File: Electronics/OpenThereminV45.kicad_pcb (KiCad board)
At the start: 2 copper layers, 50.5 x 128.5 mm, 107 parts, among them J1 USB_C_Receptacle 12401610E4#2A, J2 Conn_02x03_Odd_Even, J3 Conn_02x05_Odd_Even, P1 10k, P10 BUTTON, P11 A3_PAD, P12 A2_PAD, P13 A1_PAD, P14 A0_PAD, P16 GND, P2 10k, P3 10k, P4 10k, P8 VCC, P9 GND, U1 TTP223, U10 CH340G, U11 LP2985-3.3, U12 MCP4922-E/SL, U2 74HC4060D, U3 74HC4060D, U4 74HC74, U5 HEF4069, U6 MCP4921-E/SN, U7 MCP4922-E/SL, U8 MCP6002T-I/SN, U9 ATmega328P-AU, X1 16MHz, X2 7.3721MHz, Y1 MountPad3, Y2 MountPad3, Y3 PLUG_3_5_SMD SJ-3502-SMT-TR, Y7 PLUG_3_5_SMD SJ-3502-SMT-TR

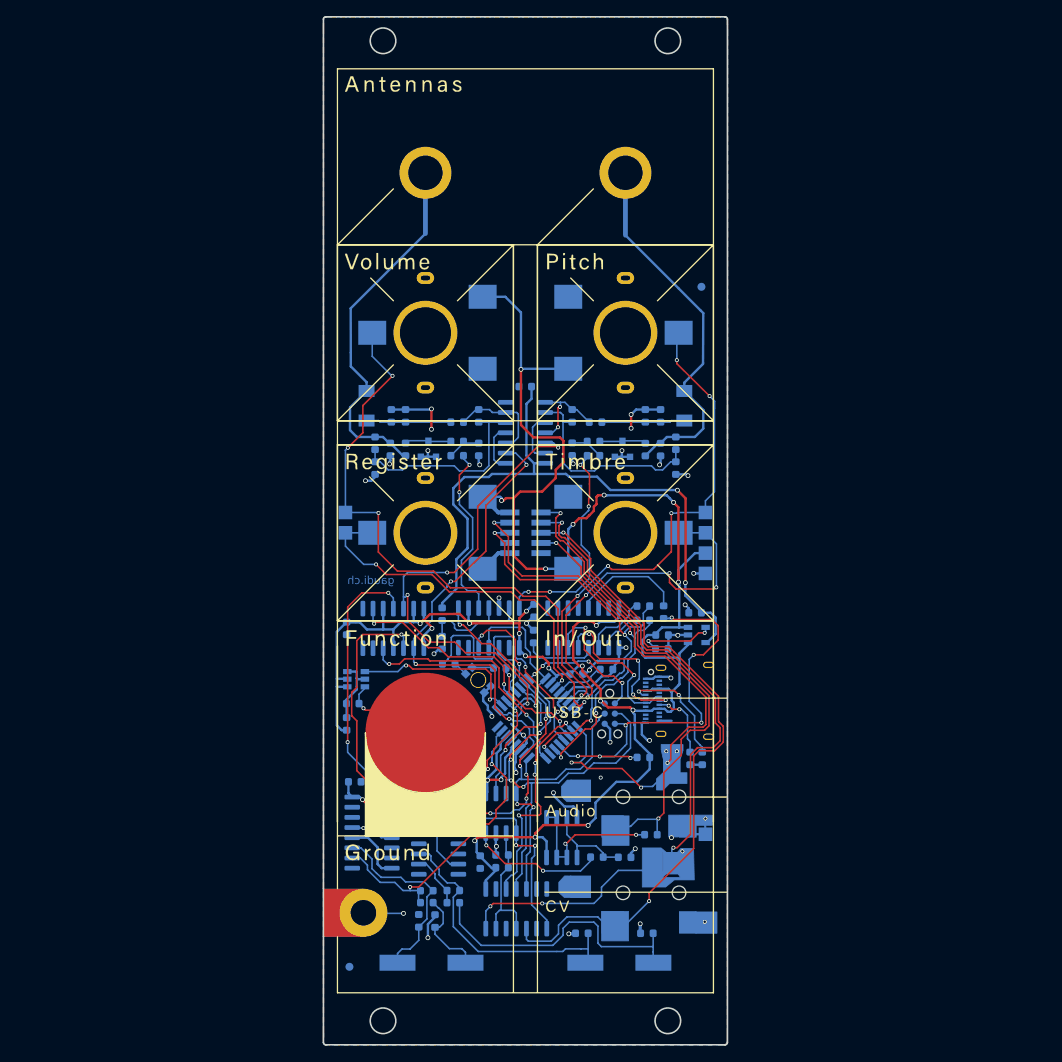
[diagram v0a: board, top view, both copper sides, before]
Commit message: changed to 4-layer and added esd protection and bypass caps
not final yet, audio connector has wrong footprint
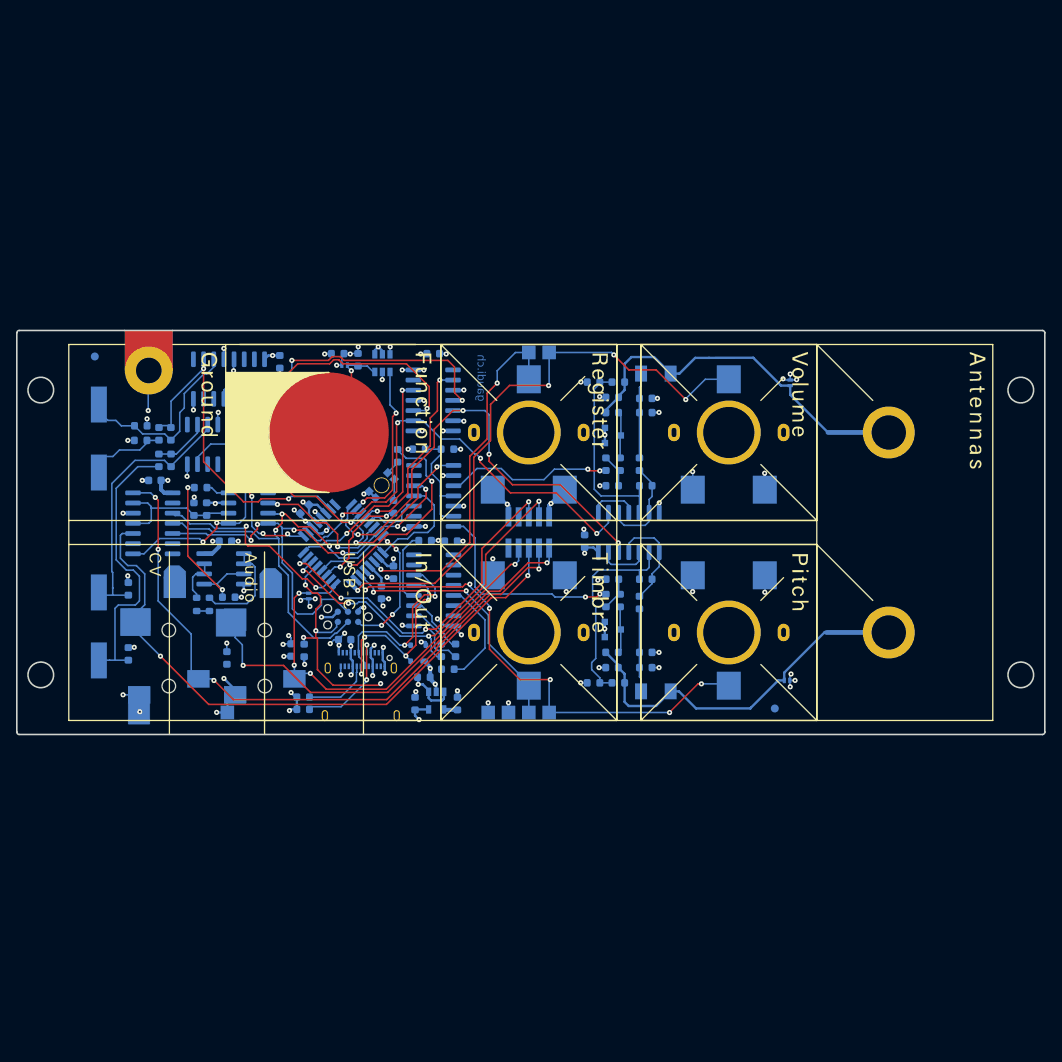
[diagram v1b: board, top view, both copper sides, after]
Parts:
- added C19: 100nF, Capacitor_SMD:C_0603_1608Metric, B.Cu at (72.4, 97.8)
- added C31: 100nF, Capacitor_SMD:C_0603_1608Metric, B.Cu at (62.5, 101.8)
- added C39: 100nF, Capacitor_SMD:C_0603_1608Metric, B.Cu at (53.7, 94.2)
- added C40: 100n, Capacitor_SMD:C_0603_1608Metric, B.Cu at (77.4, 114.1)
- added C41: 10u, Capacitor_SMD:C_0603_1608Metric, B.Cu at (70.7, 115.4)
- added D4: PRTR5V0U2X, Package_TO_SOT_SMD:SOT-143, B.Cu at (86.6, 115.8)
- added D5: PESD5V0X1BL, Diode_SMD:D_SOD-882, B.Cu at (72.9, 108.7)
- added D6: PESD5V0X1BL, Diode_SMD:D_SOD-882, B.Cu at (132.7, 119.2)
- added D7: PESD5V0X1BL, Diode_SMD:D_SOD-882, B.Cu at (133.1, 82.0)
- added D8: PESD5V0X1BL, Diode_SMD:D_SOD-882, B.Cu at (77.4, 79.8)
- added R23: 10R, Resistor_SMD:R_0603_1608Metric, B.Cu at (60.5, 109.7)
- added R24: 10R, Resistor_SMD:R_0603_1608Metric, B.Cu at (58.9, 109.7)
- D3: value DualLED 156125RB73000 -> DualLED 156125RB73000
- J1: value USB_C_Receptacle 12401610E4#2A -> USB_C_Receptacle 12401610E4#2A
- U10: value CH340G -> CH340C
- U4: value 74HC74 -> 74HC74D
- Y3, Y7: value PLUG_3_5_SMD SJ-3502-SMT-TR -> PLUG_3_5_SMD SJ-3502-SMT-TR
- moved G*** 87.3 mm to (162.0, 100.7), turned to -90 degrees
- moved G*** 86.2 mm to (39.3, 100.7), turned to 90 degrees
- moved W2 82.7 mm to (46.2, 78.7), turned to -90 degrees
- moved X1 77.6 mm to (46.7, 89.0), turned to -90 degrees
- moved X2 77.5 mm to (46.7, 112.5), turned to -90 degrees
- moved G*** 76.1 mm to (154.0, 101.0), turned to 90 degrees
- moved G*** 75.7 mm to (46.7, 100.7), turned to 90 degrees
- moved C18 73.6 mm to (50.4, 115.9), turned to 90 degrees
- moved GROUND1 72.9 mm to (52.9, 80.5), turned to -90 degrees
- moved C17 71.2 mm to (50.4, 107.8), turned to 90 degrees
- moved C15 71.0 mm to (51.9, 87.4), turned to 0 degrees
- moved Y3 70.9 mm to (55.4, 123.4), turned to 90 degrees
- moved C16 70.4 mm to (51.9, 89.2), turned to 180 degrees
- moved R17 67.7 mm to (59.4, 95.1), turned to 180 degrees
- moved R12 67.5 mm to (54.2, 88.4), turned to 90 degrees
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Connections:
- C29 pad 1: Net-(C29-Pad1) -> AUDIO
- C29 pad 2: AUDIO -> Net-(Y7-L)
- J1 pad S1: unconnected-(J1-PadS1) -> GND
- J3 pad 8: D- -> unconnected-(J3-Pin_8-Pad8)
- J3 pad 9: D+ -> unconnected-(J3-Pin_9-Pad9)
- U8 pad 1: Net-(C29-Pad1) -> Net-(U8A--)
- U8 pad 2: Net-(C29-Pad1) -> Net-(U8A--)
- U8 pad 6: Net-(C29-Pad1) -> Net-(U8B--)
- U8 pad 7: Net-(C29-Pad1) -> Net-(U8B--)
- Y7 pad 3: AUDIO -> Net-(Y7-L)
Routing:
- net VCC: track 331.1 -> 73.1 mm, vias 26 -> 36
- net RESET: track 50.5 -> 30.1 mm, vias 7 -> 4
- net Net-(C29-Pad1): track 19.7 -> 0.00 mm, vias 2 -> 0
- net A2: track 48.9 -> 33.1 mm, vias 4 -> 2
- net VDD: track 81.9 -> 67.8 mm, vias 2 -> 3
- net Net-(U6-VoutA): track 17.0 -> 2.97 mm, vias 2 -> 0
- net Net-(U8A--): track 0.00 -> 12.9 mm
- net Net-(U8A-+): track 11.5 -> 22.8 mm, vias 0 -> 2
- net GND: track 130.3 -> 119.6 mm, vias 36 -> 85
- net GATE: track 63.7 -> 54.3 mm
- net Net-(U11-BP): track 9.51 -> 1.72 mm, vias 2 -> 0
- net CV1: track 88.6 -> 81.2 mm, vias 5 -> 4
- net Net-(U8B--): track 0.00 -> 5.66 mm
- net LED_RED: track 33.3 -> 28.1 mm
- net CV2: track 83.8 -> 78.8 mm
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- added copper zone on In1.Cu, net GND
- added copper zone on In2.Cu, net VCC
- removed copper zone on B.Cu, net GND
- removed copper zone on F.Cu, net GND
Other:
- board size 50.5 x 128.5 mm -> 128.5 x 50.5 mm
- copper layers 2 -> 4

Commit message: Added some text; moved some reference descriptors; pcb layer identification
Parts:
- moved R23 3.04 mm to (60.0, 112.7)
- moved R24 1.10 mm to (60.0, 109.7)
- moved C41 0.91 mm to (71.6, 115.5)
- moved R20 0.76 mm to (73.1, 115.5)
- moved C22 0.42 mm to (62.5, 108.7)
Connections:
- C29 pad 1: AUDIO -> Net-(C29-Pad1)
- C29 pad 2: Net-(Y7-L) -> AUDIO
- R23 pad 1: AUDIO -> Net-(C29-Pad1)
- R24 pad 1: AUDIO -> Net-(C29-Pad1)
- Y7 pad 3: Net-(Y7-L) -> AUDIO
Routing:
- net Net-(C29-Pad1): track 0.00 -> 7.48 mm
- net GND: track 119.6 -> 124.5 mm
- net AUDIO: track 58.6 -> 56.3 mm, vias 3 -> 2
- net VCC: track 73.1 -> 75.0 mm
- net DAC_DI: track 60.7 -> 59.2 mm
- net Net-(U8A--): track 12.9 -> 13.8 mm
- net Net-(U8B--): track 5.66 -> 6.29 mm
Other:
- board text added: "2"
- board text added: "3"
- board text added: "IDcircuits edition V4.5 2025"
- board text added: "bottom 4"
- board text added: "top 1"
- board text removed: "V4.5 2023"

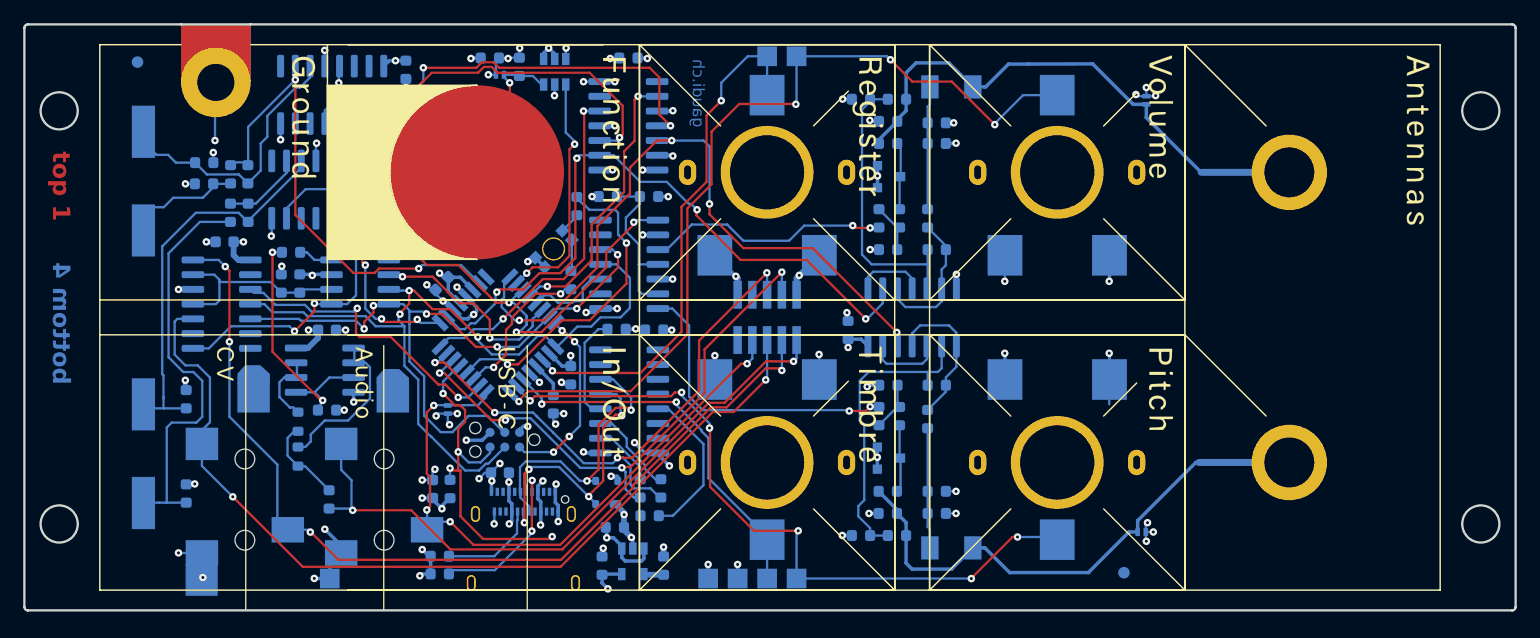
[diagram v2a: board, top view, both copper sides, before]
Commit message: 4-layer version; 3D updates and more
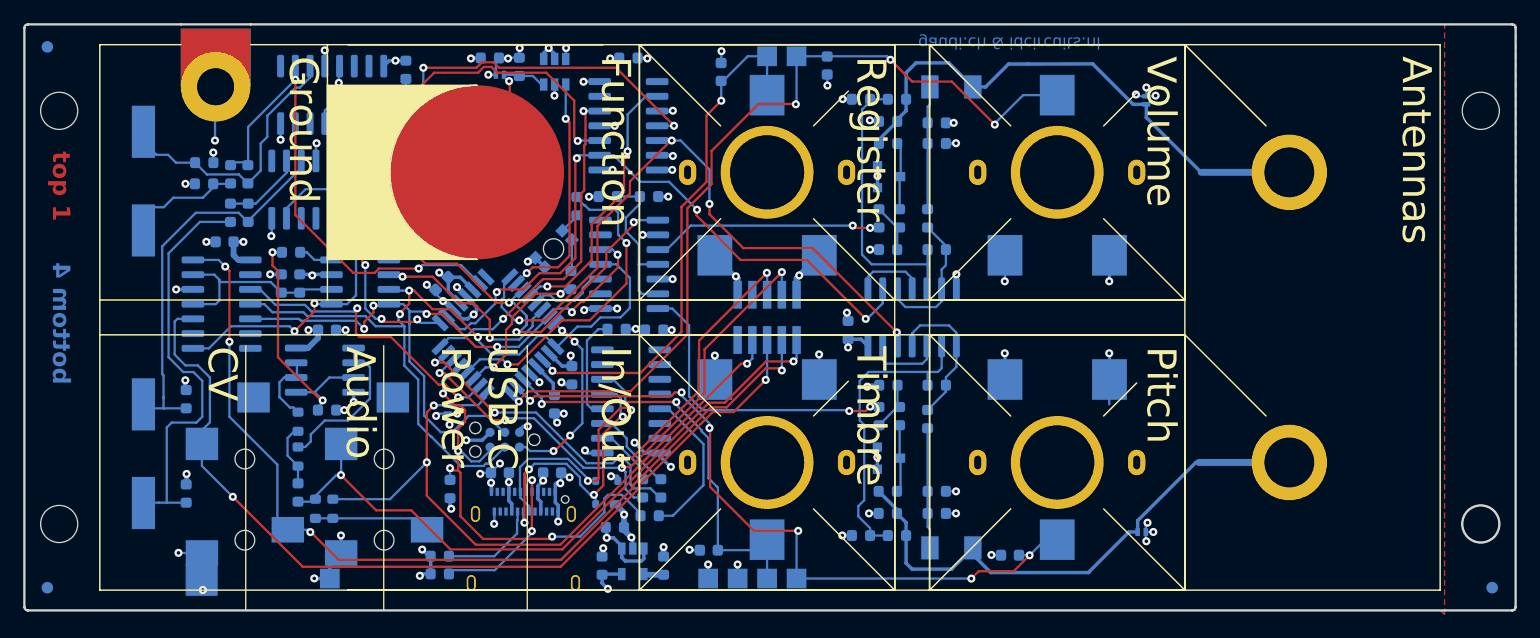
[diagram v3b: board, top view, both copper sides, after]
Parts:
- removed the G*** at (104.4, 97.5)
- removed W1: FIDUCIAL1, GaudiLabsFootPrints:Fiducial_1mm_Dia_2.54mm_Outer_CopperBottom
- removed W2: FIDUCIAL2, GaudiLabsFootPrints:Fiducial_1mm_Dia_2.54mm_Outer_CopperBottom
- added C42: 100n, Capacitor_SMD:C_0603_1608Metric, B.Cu at (121.3, 121.2)
- added C43: 100n, Capacitor_SMD:C_0603_1608Metric, B.Cu at (105.6, 79.0)
- added C44: 100n, Capacitor_SMD:C_0603_1608Metric, B.Cu at (95.4, 120.8)
- added C45: 100n, Capacitor_SMD:C_0603_1608Metric, B.Cu at (96.5, 79.6)
- added FID1: Fiducial, Fiducial:Fiducial_1mm_Mask3mm, B.Cu at (38.4, 77.4)
- added FID2: Fiducial, Fiducial:Fiducial_1mm_Mask3mm, B.Cu at (162.9, 124.0)
- added FID3: Fiducial, Fiducial:Fiducial_1mm_Mask3mm, B.Cu at (38.4, 124.0)
- added H1: MountingHole, MountingHole:MountingHole_3.2mm_M3, F.Cu at (161.9, 82.9)
- added H2: MountingHole, MountingHole:MountingHole_3.2mm_M3, F.Cu at (161.9, 118.5)
- added H3: MountingHole, MountingHole:MountingHole_3.2mm_M3, F.Cu at (39.4, 82.9)
- added H4: MountingHole, MountingHole:MountingHole_3.2mm_M3, F.Cu at (39.4, 118.5)
- added R25: 0R, Resistor_SMD:R_0603_1608Metric, B.Cu at (61.5, 117.2)
- added R26: 0R, Resistor_SMD:R_0603_1608Metric, B.Cu at (63.0, 117.2)
- C36, C37, C41: value 10u -> 10uF
- J1: value USB_C_Receptacle 12401610E4#2A -> 12401610E4#2A
- L1, L2: footprint GaudiLabsFootPrints:COIL_T -> theremin-footprints:COIL_T
- P1, P2, P3, P4: value 10k -> PS15NV60-103A3030; footprint GaudiLabsFootPrints:PS15NV60 -> theremin-footprints:PS15NV60
- U1: value TTP223 -> TTP223E-BA6
- U11: value LP2985-3.3 -> LP2985-3.3DBV
- U5: value HEF4069 -> HEF4069UBT
- U9: value ATmega328P-AU -> ATMEGA328P-AU
- X1: value 16MHz -> 16MHz/30ppm/18pF
- X2: value 7.3721MHz -> 7.3721MHz/30ppm/18pF
- Y3, Y7: value PLUG_3_5_SMD SJ-3502-SMT-TR -> SJ-3523-SMT-TR
- moved C41 10.4 mm to (81.9, 114.1), turned to 0 degrees
- moved C29 2.75 mm to (60.0, 115.8)
- moved GROUND1 0.37 mm to (52.9, 80.8)
- moved R9 0.21 mm to (89.7, 115.4)
- moved U10 0.17 mm to (88.7, 107.9)
- moved C23 0.10 mm to (83.6, 105.7)
- moved C33 0.10 mm to (82.1, 108.2)
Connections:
- Y7 pad 2: GATE -> Net-(Y7-R)
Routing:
- net RESET: track 29.6 -> 40.0 mm
- net Net-(Y7-R): track 0.00 -> 10.1 mm
- net GATE: track 54.5 -> 61.4 mm, vias 4 -> 3
- net A2: track 33.1 -> 36.8 mm
- net Net-(U3-Q4): track 43.3 -> 39.7 mm
- net VCC: track 75.0 -> 71.8 mm, vias 36 -> 33
- net GND: track 124.5 -> 126.6 mm, vias 85 -> 87
- net Net-(C29-Pad1): track 7.48 -> 5.42 mm
- net VO_PITCH: track 60.2 -> 58.3 mm
- net AUDIO: track 56.3 -> 57.8 mm
- net Net-(U2-Q5): track 38.6 -> 37.5 mm
- net VoutB: track 21.2 -> 20.0 mm
- net A1: track 75.1 -> 74.1 mm
- net A0: track 61.7 -> 62.4 mm
- added copper zone on F.Cu, net (none)
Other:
- outline, holes or cut-outs redrawn
- board text added: "Antennas"
- board text added: "Audio"
- board text added: "CV"
- board text added: "Function"
- board text added: "Ground"
- board text added: "IDcircuits edition V4.5.1 2025"
- board text added: "In/Out"
- board text added: "Pitch"
- board text added: "Register"
- board text added: "Timbre"
- board text added: "USB-C Power"
- board text added: "Volume"
- board text added: "gaudi.ch & idcircuits.nl"
- board text removed: "GATE"
- board text removed: "IDcircuits edition V4.5 2025"
- board text removed: "gaudi.ch"
